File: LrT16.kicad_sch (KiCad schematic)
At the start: 200 parts, among them J1 USB_C_Receptacle_USB2.0, J2 Conn_02x05_Odd_Even, Q1 2N7002, Q2 2N7002, SW1 EC11_SMD, SW10 EC11_SMD, SW11 EC11_SMD, SW12 EC11_SMD, SW13 EC11_SMD, SW14 EC11_SMD, SW15 EC11_SMD, SW16 EC11_SMD, SW17 SW_Push, SW18 SW_Push, SW2 EC11_SMD, SW20 SW_SPST, SW3 EC11_SMD, SW4 EC11_SMD, SW5 EC11_SMD, SW6 EC11_SMD, SW7 EC11_SMD, SW8 EC11_SMD, SW9 EC11_SMD, U1 STM32F072C8Tx, U2 SPX3819M5-L3-3TR

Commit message: edit pcb pattern
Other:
- title: LrT16 0.1 -> LrT16 F1.2

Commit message: modify schematic for encoder
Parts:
- added C38, C58, C59, C60, C61, C62, C63, C64, C65, C66, C67, C68, C69, C70, C71, C72, C73: 33n, Capacitor_SMD:C_0603_1608Metric, symbol LrE-6-rescue:C-Device
- added R60, R61, R62, R63, R64, R65, R66, R67, R68, R69, R70, R71, R72, R73, R74, R75, R76, R77, R84, R85, R86, R87, R88, R89, R90, R91: 1K, Resistor_SMD:R_0603_1608Metric, symbol LrE-6-rescue:R-Device
- added R78, R79, R80, R81, R82, R83: 1K, Resistor_SMD:R_0603_1608Metric, symbol Device:R
- C1, C10, C11, C12, C13, C14, C15, C16, C17, C18, C19, C2, C20, C21, C22, C23, C24, C25, C26, C27, C28, C29, C3, C30, C31, C32, C36, C37, C4, C5, C6, C7, C8, C9: footprint Capacitor_SMD:C_0805_2012Metric -> Capacitor_SMD:C_0603_1608Metric
- D1, D10, D11, D12, D13, D14, D15, D16, D17, D18, D19, D2, D20, D21, D22, D23, D24, D25, D26, D27, D28, D29, D3, D30, D31, D32, D33, D34, D35, D36, D37, D38, D39, D4, D40, D41, D42, D43, D44, D45, D46, D47, D48, D5, D58, D6, D7, D8, D9: value 1N4148W -> 1N4148WS; footprint Diode_SMD:D_SOD-123 -> Diode_SMD:D_SOD-523
- R1, R10, R11, R12, R13, R14, R15, R16, R17, R18, R19, R2, R20, R21, R22, R23, R24, R25, R26, R27, R28, R29, R3, R30, R31, R32, R33, R34, R36, R38, R39, R4, R40, R41, R42, R43, R44, R45, R46, R47, R48, R49, R5, R50, R51, R52, R53, R54, R55, R56, R6, R7, R8, R9: footprint Resistor_SMD:R_0805_2012Metric -> Resistor_SMD:R_0603_1608Metric
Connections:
- net GND: now also C38.2, C58.2, C59.2, C60.2, C61.2, C62.2, C63.2, C64.2, C65.2, C66.2, C67.2, C68.2, C69.2, C70.2, C71.2, C72.2, C73.2, R60.2, R61.2, R62.2, R63.2, R64.2, R65.2, R66.2, R67.2, R68.2, R69.2, R70.2, R71.2, R72.2, R73.2, R74.2, R75.2, R76.2, R77.2, R78.1, R79.1, R80.1, R81.1, R82.1, R83.1, R84.2, R85.2, R86.2, R87.2, R88.2, R89.2, R90.2, R91.2; no longer SW1.C, SW10.C, SW11.C, SW12.C, SW13.C, SW14.C, SW15.C, SW16.C, SW2.C, SW3.C, SW4.C, SW5.C, SW6.C, SW7.C, SW8.C, SW9.C
- net L0: no longer R10.1, R12.1, R14.1, R16.1, R2.1, R4.1, R6.1, R8.1
- net L1: no longer R18.1, R20.1, R22.1, R24.1, R26.1, R28.1, R30.1, R32.1
- net L2: now also R10.1, R12.1, R14.1, R16.1, R18.1, R2.1, R20.1, R22.1, R24.1, R26.1, R28.1, R30.1, R32.1, R4.1, R6.1, R8.1; no longer SW1.S1, SW10.S1, SW11.S1, SW12.S1, SW13.S1, SW14.S1, SW15.S1, SW16.S1, SW2.S1, SW3.S1, SW4.S1, SW5.S1, SW6.S1, SW7.S1, SW8.S1, SW9.S1
- net M0: no longer R40.2
- net M1: no longer R41.2
- net M10: no longer R50.2
- net M11: no longer R51.2
- net M12: no longer R52.2
- net M13: no longer R53.2
- net M14: no longer R54.2
- net M15: no longer R55.2
- net M2: no longer R42.2
- net M3: no longer R43.2
- net M4: no longer R44.2
- net M5: no longer R45.2
- net M6: no longer R46.2
- net M7: no longer R47.2
- net M8: no longer R48.2
- net M9: no longer R49.2
- net at C19.1, D29.2 (A), SW10.A: now also R78.2; no longer R19.2
- net at C20.1, D30.2 (A), SW10.B: now also R79.2; no longer R20.2
- net at D28.2 (A): now also R20.2, SW10.S1; no longer SW10.S2
- net at C21.1, D32.2 (A), SW11.A: now also R80.2; no longer R21.2
- net at C22.1, D33.2 (A), SW11.B: now also R81.2; no longer R22.2
- net at D31.2 (A): now also R22.2, SW11.S1; no longer SW11.S2
- net at C23.1, D35.2 (A), SW12.A: now also R82.2; no longer R23.2
- net at C24.1, D36.2 (A), SW12.B: now also R83.2; no longer R24.2
- net at D34.2 (A): now also R24.2, SW12.S1; no longer SW12.S2
- net at C25.1, D38.2 (A), SW13.A: now also R84.1; no longer R25.2
- net at C26.1, D39.2 (A), SW13.B: now also R85.1; no longer R26.2
- net at D37.2 (A): now also R26.2, SW13.S1; no longer SW13.S2
- net at C27.1, D41.2 (A), SW14.A: now also R86.1; no longer R27.2
- net at C28.1, D42.2 (A), SW14.B: now also R87.1; no longer R28.2
- net at D40.2 (A): now also R28.2, SW14.S1; no longer SW14.S2
- net at C17.1, D26.2 (A), SW9.A: now also R76.1; no longer R17.2
- net at C18.1, D27.2 (A), SW9.B: now also R77.1; no longer R18.2
- net at D25.2 (A): now also R18.2, SW9.S1; no longer SW9.S2
- net at C29.1, D44.2 (A), SW15.A: now also R88.1; no longer R29.2
- net at C30.1, D45.2 (A), SW15.B: now also R89.1; no longer R30.2
- net at D43.2 (A): now also R30.2, SW15.S1; no longer SW15.S2
- net at C31.1, D47.2 (A), SW16.A: now also R90.1; no longer R31.2
- net at C32.1, D48.2 (A), SW16.B: now also R91.1; no longer R32.2
- net at D46.2 (A): now also R32.2, SW16.S1; no longer SW16.S2
- net CC1: now reaches J1.A5 (CC1), R34.1
- net CC2: now reaches J1.B5 (CC2), R33.1
- net at C11.1, D17.2 (A), SW6.A: now also R70.1; no longer R11.2
- net at C6.1, D9.2 (A), SW3.B: now also R65.1; no longer R6.2
- net at C7.1, D11.2 (A), SW4.A: now also R66.1; no longer R7.2
- net at C8.1, D12.2 (A), SW4.B: now also R67.1; no longer R8.2
- net at D10.2 (A): now also R8.2, SW4.S1; no longer SW4.S2
- net at C13.1, D20.2 (A), SW7.A: now also R72.1; no longer R13.2
- net at C14.1, D21.2 (A), SW7.B: now also R73.1; no longer R14.2
- net at D19.2 (A): now also R14.2, SW7.S1; no longer SW7.S2
- net at D16.2 (A): now also R12.2, SW6.S1; no longer SW6.S2
- net at C9.1, D14.2 (A), SW5.A: now also R68.1; no longer R9.2
- net at C10.1, D15.2 (A), SW5.B: now also R69.1; no longer R10.2
- net at C2.1, D3.2 (A), SW1.B: now also R61.1; no longer R2.2
- net at C4.1, D6.2 (A), SW2.B: now also R63.1; no longer R4.2
- net at C5.1, D8.2 (A), SW3.A: now also R64.1; no longer R5.2
- net at C1.1, D2.2 (A), SW1.A: now also R60.1; no longer R1.2
- net at C15.1, D23.2 (A), SW8.A: now also R74.1; no longer R15.2
- net at C3.1, D5.2 (A), SW2.A: now also R62.1; no longer R3.2
- net at SW2.S2: now also R41.2, C71.1; no longer D4.2 (A)
- net at D58.2 (A), LS1.2, R57.1: now also C38.1
- net at C12.1, D18.2 (A), SW6.B: now also R71.1; no longer R12.2
- net at C16.1, D24.2 (A), SW8.B: now also R75.1; no longer R16.2
- net at D1.2 (A): now also R2.2, SW1.S1; no longer SW1.S2
- net at SW8.S2: now also R47.2, C62.1; no longer D22.2 (A)
- net at D13.2 (A): now also R10.2, SW5.S1; no longer SW5.S2
- net at SW3.S2: now also R42.2, C58.1; no longer D7.2 (A)
- new net: R19.2, SW10.C
- new net: C63.1, R49.2, SW10.S2
- new net: R21.2, SW11.C
- new net: C64.1, R50.2, SW11.S2
- new net: R23.2, SW12.C
- new net: C65.1, R51.2, SW12.S2
- new net: R25.2, SW13.C
- new net: C66.1, R52.2, SW13.S2
- new net: R27.2, SW14.C
- new net: C67.1, R53.2, SW14.S2
- new net: R17.2, SW9.C
- new net: C73.1, R48.2, SW9.S2
- new net: R29.2, SW15.C
- new net: C68.1, R54.2, SW15.S2
- new net: R31.2, SW16.C
- new net: C69.1, R55.2, SW16.S2
- new net: R7.2, SW4.C
- new net: C59.1, R43.2, SW4.S2
- new net: R13.2, SW7.C
- new net: C61.1, R46.2, SW7.S2
- new net: R9.2, SW5.C
- new net: C60.1, R45.2, SW6.S2
- new net: D4.2 (A), R4.2, SW2.S1
- new net: C70.1, R40.2, SW1.S2
- new net: R1.2, SW1.C
- new net: R5.2, SW3.C
- new net: R3.2, SW2.C
- new net: D7.2 (A), R6.2, SW3.S1
- new net: R11.2, SW6.C
- new net: R15.2, SW8.C
- new net: D22.2 (A), R16.2, SW8.S1
- new net: C72.1, R44.2, SW5.S2
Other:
- moved on the sheet: C1, C10, C11, C12, C13, C14, C15, C16, C17, C18, C19, C2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

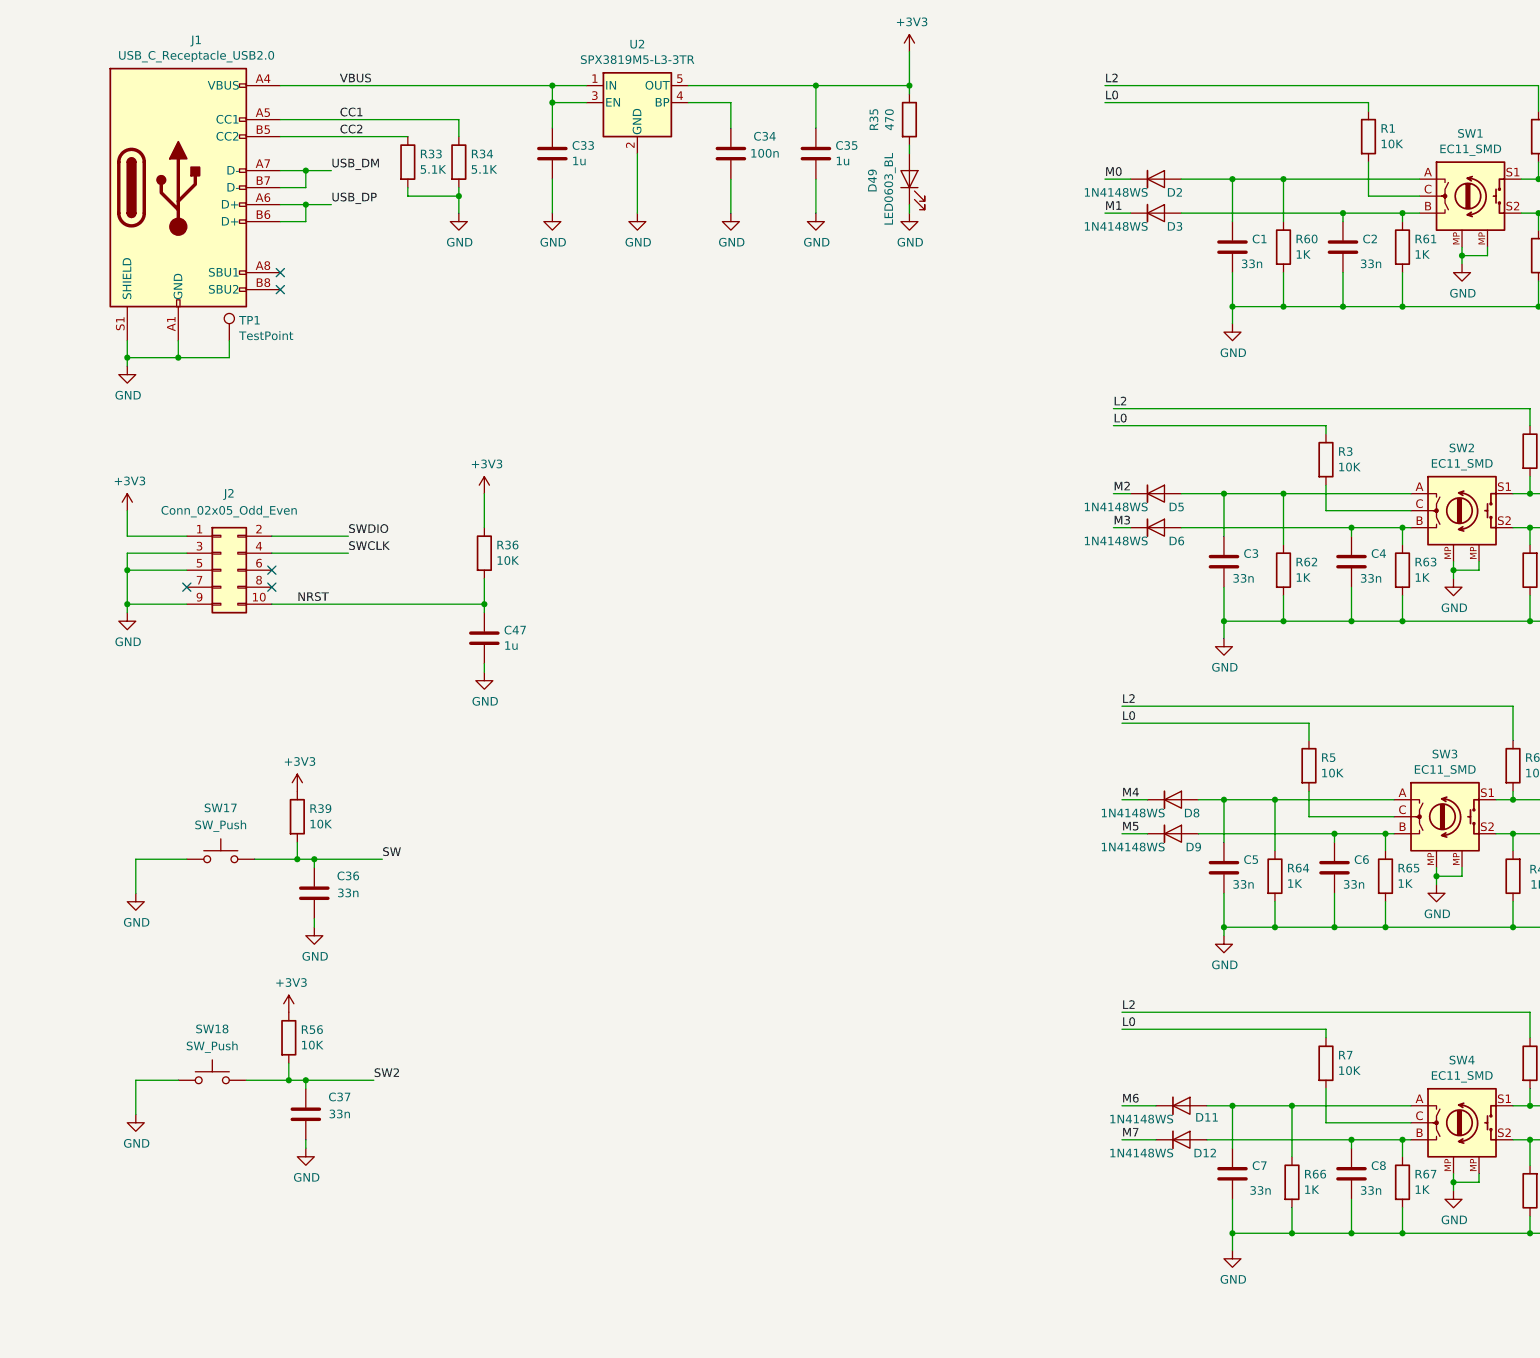
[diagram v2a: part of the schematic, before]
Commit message: fixed scematic for footprint on top side
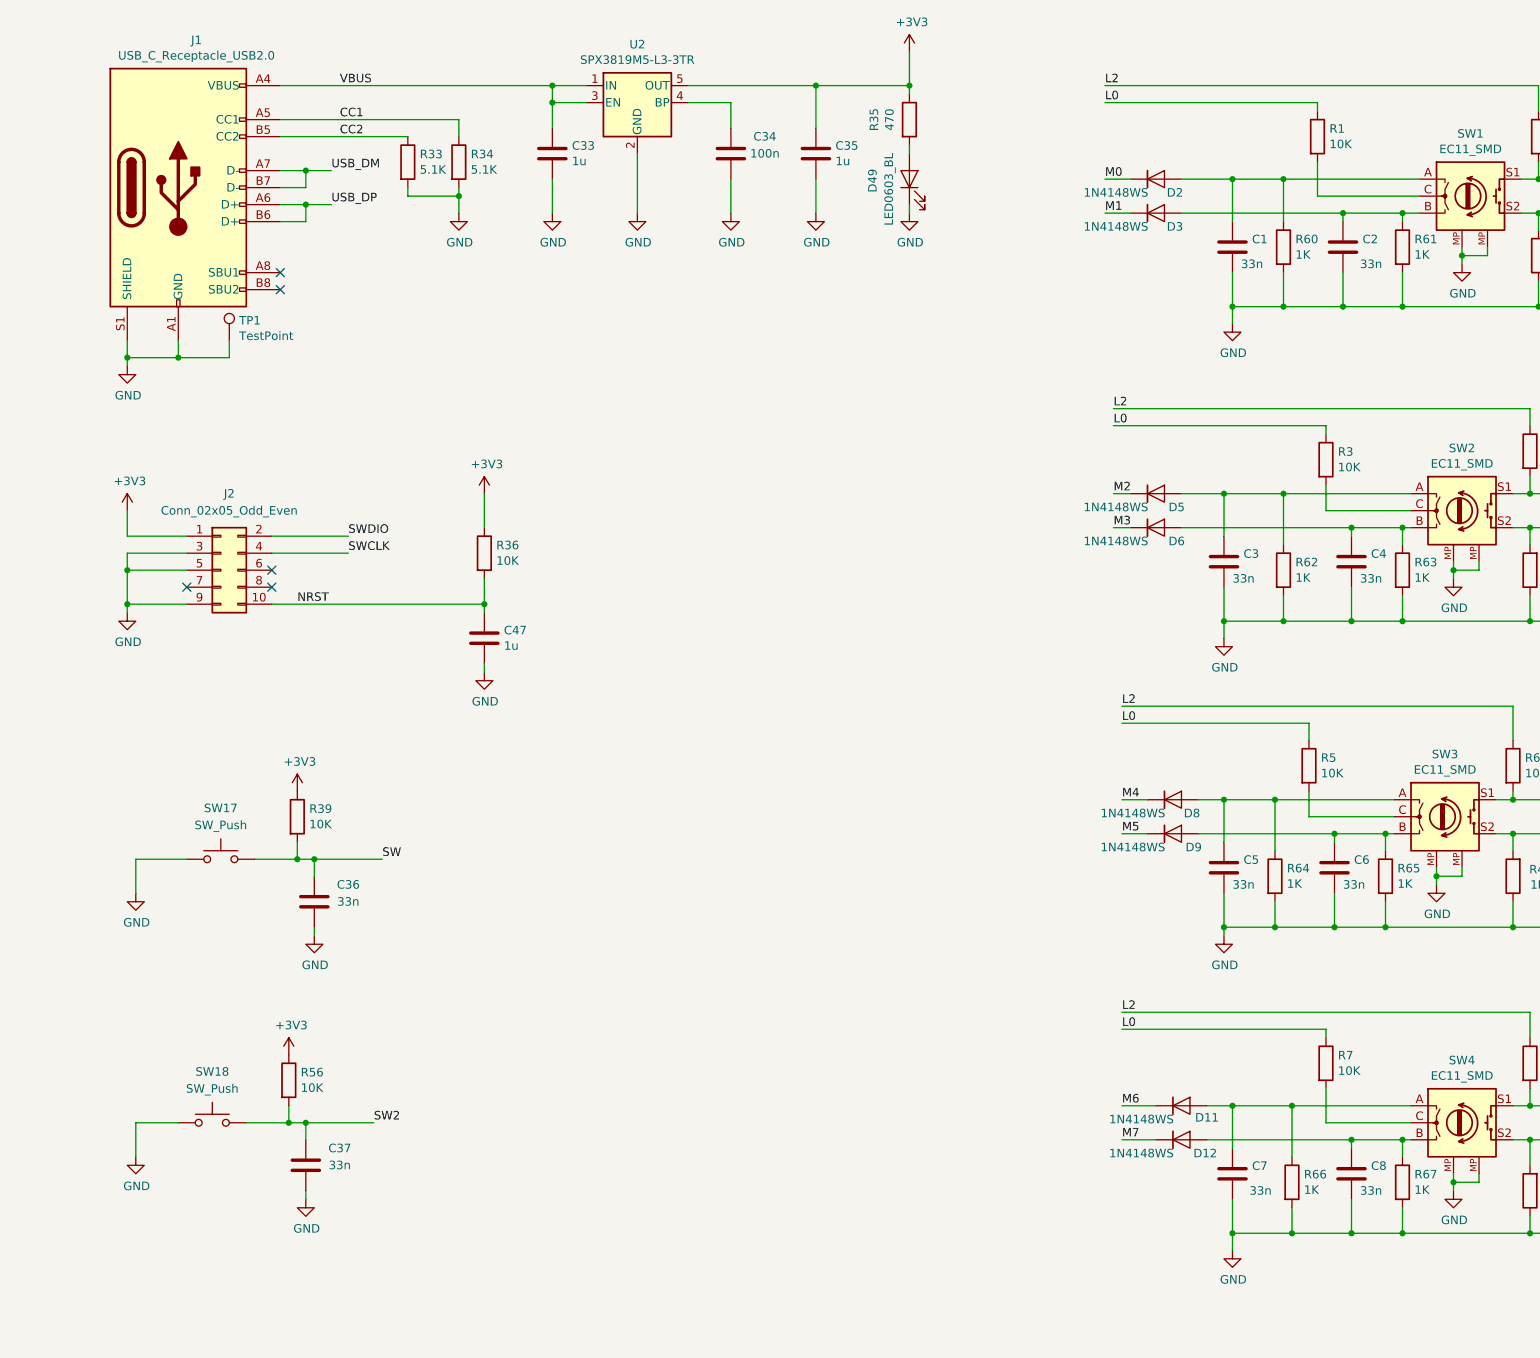
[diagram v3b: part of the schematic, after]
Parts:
- C48, C50, C51, C52, C53, C54, C55, C56, C57: footprint Capacitor_SMD:C_0805_2012Metric -> Capacitor_SMD:C_0603_1608Metric
- D49: footprint LED_SMD:LED_0603_1608Metric -> LED_SMD:LED_0603_1608Metric_Pad1.05x0.95mm_HandSolder
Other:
- moved on the sheet: C36, C37, R1, R56, SW18

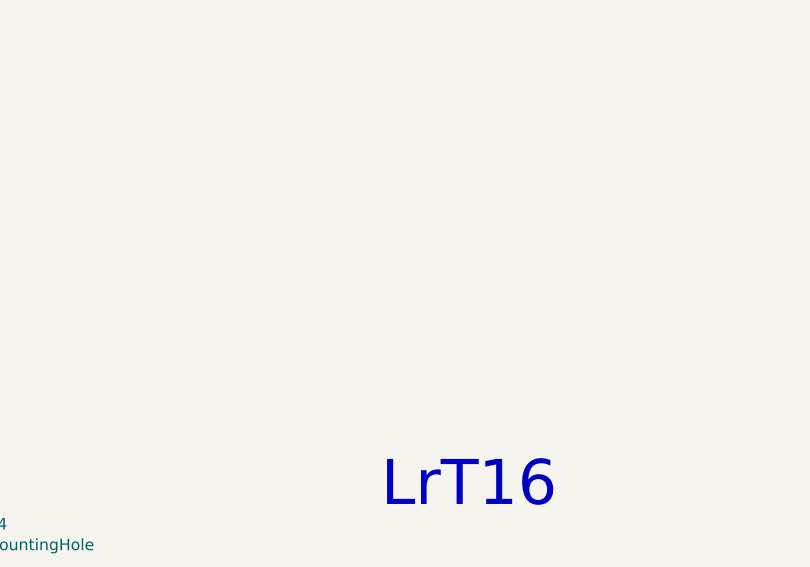
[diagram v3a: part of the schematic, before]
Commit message: Ready for PCB order
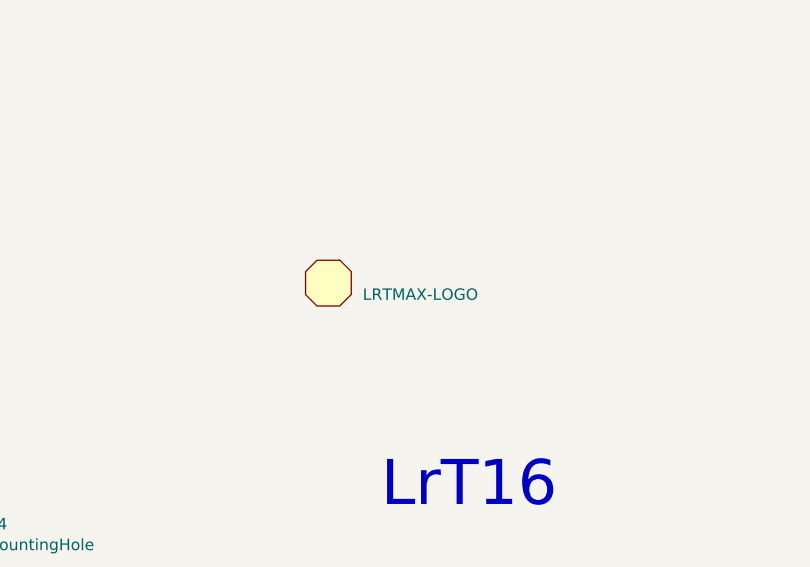
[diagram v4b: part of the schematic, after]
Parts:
- added REF01: LRTMAX-LOGO, LrE-6:LrTMAX-LOGO, symbol Mechanical:Mechanical_Shape
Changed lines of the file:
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@@
+	)
+	(symbol
+		(lib_id "Mechanical:Mechanical_Shape")
+		(at 478.79 361.95 0)
+		(unit 1)
+		(exclude_from_sim yes)
+		(in_bom no)
+		(on_board yes)
+		(dnp no)
+		(fields_autoplaced yes)
+		(property "Reference" "REF01"
+			(at 482.6 360.6799 0)
+			(effects
+				(font
+					(size 1.27 1.27)
+				)
+				(justify left)
+				(hide yes)
+			)
+		)
+		(property "Value" "LRTMAX-LOGO"
+			(at 482.6 363.2199 0)
+			(effects
+				(font
+					(size 1.27 1.27)
+				)
+				(justify left)
+			)
+		)
+		(property "Footprint" "LrE-6:LrTMAX-LOGO"
+			(at 478.79 367.03 0)
+			(effects
+				(font
+					(size 1.27 1.27)
+				)
+				(hide yes)
+			)
+		)
+		(property "Datasheet" "~"
+			(at 478.79 358.14 0)
+			(effects
+				(font
+					(size 1.27 1.27)
+				)
+				(hide yes)
+			)
+		)
+		(property "Description" ""
+			(at 478.79 361.95 0)
+			(effects
+				(font
+					(size 1.27 1.27)
+				)
+				(hide yes)
+			)
+		)
+		(instances
+			(project "LrT16"
+				(path "/b873bc5d-a9af-4bd9-afcb-87ce4d417120"
+					(reference "REF01")
+					(unit 1)
+				)
+			)
+		)
 	)
 	(symbol

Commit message: Mod. switch debouncer
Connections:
- net at D28.2 (A), R20.2, SW10.S1: now also C63.1
- net at R49.2, SW10.S2: no longer C63.1
- net at D31.2 (A), R22.2, SW11.S1: now also C64.1
- net at R50.2, SW11.S2: no longer C64.1
- net at D34.2 (A), R24.2, SW12.S1: now also C65.1
- net at R51.2, SW12.S2: no longer C65.1
- net at D37.2 (A), R26.2, SW13.S1: now also C66.1
- net at R52.2, SW13.S2: no longer C66.1
- net at D40.2 (A), R28.2, SW14.S1: now also C67.1
- net at R53.2, SW14.S2: no longer C67.1
- net at D25.2 (A), R18.2, SW9.S1: now also C73.1
- net at R48.2, SW9.S2: no longer C73.1
- net at D43.2 (A), R30.2, SW15.S1: now also C68.1
- net at R54.2, SW15.S2: no longer C68.1
- net at D46.2 (A), R32.2, SW16.S1: now also C69.1
- net at R55.2, SW16.S2: no longer C69.1
- net at R41.2, SW2.S2: no longer C71.1
- net at D10.2 (A), R8.2, SW4.S1: now also C59.1
- net at R43.2, SW4.S2: no longer C59.1
- net at D19.2 (A), R14.2, SW7.S1: now also C61.1
- net at R46.2, SW7.S2: no longer C61.1
- net at R42.2, SW3.S2: no longer C58.1
- net at D16.2 (A), R12.2, SW6.S1: now also C60.1
- net at D13.2 (A), R10.2, SW5.S1: now also C72.1
- net at R47.2, SW8.S2: no longer C62.1
- net at D1.2 (A), R2.2, SW1.S1: now also C70.1
- net at R45.2, SW6.S2: no longer C60.1
- net at D4.2 (A), R4.2, SW2.S1: now also C71.1
- net at R40.2, SW1.S2: no longer C70.1
- net at D7.2 (A), R6.2, SW3.S1: now also C58.1
- net at D22.2 (A), R16.2, SW8.S1: now also C62.1
- net at R44.2, SW5.S2: no longer C72.1
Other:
- moved on the sheet: D1, D10, D13, D16, D19, D22, D25, D28, D31, D34, D37, D4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

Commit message: Ready for F1.2 PCB order
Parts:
- C33, C34, C35, D49, D50, D51, D52, D53, D54, D55, D56, D57, J1, J2, LS1, SW1, SW10, SW11, SW12, SW13, SW14, SW15, SW16, SW17, SW18, SW2, SW20, SW3, SW4, SW5, SW6, SW7, SW8, SW9, TP1, U1, U2: now left out of the parts list
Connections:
- net GND: now also SW17.G1, SW17.G2, SW18.G1, SW18.G2
